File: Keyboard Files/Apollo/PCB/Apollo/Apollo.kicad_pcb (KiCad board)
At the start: 2 copper layers, 309.8 x 159.1 mm, 198 parts, among them J1 AVR-ISP-6, J10 Conn_01x01, J11 Conn_01x01, J12 Conn_01x01, J13 Conn_01x01, J14 Conn_01x01, J15 Conn_01x01, J16 Conn_01x01, J2 AVR-ISP-6, J3 Conn_01x01, J4 Conn_01x01, J5 Conn_01x01, J6 Conn_01x01, J7 Conn_01x01, J8 Conn_01x01, J9 Conn_01x01, SW1 SW_Push, SW2 SW_Push, U1 PRTR5V0U2X, U2 ATmega32U4-MU, U3 PRTR5V0U2X, U4 ATmega32U4-MU, Y1 Crystal_GND24_Small, Y2 Crystal_GND24_Small

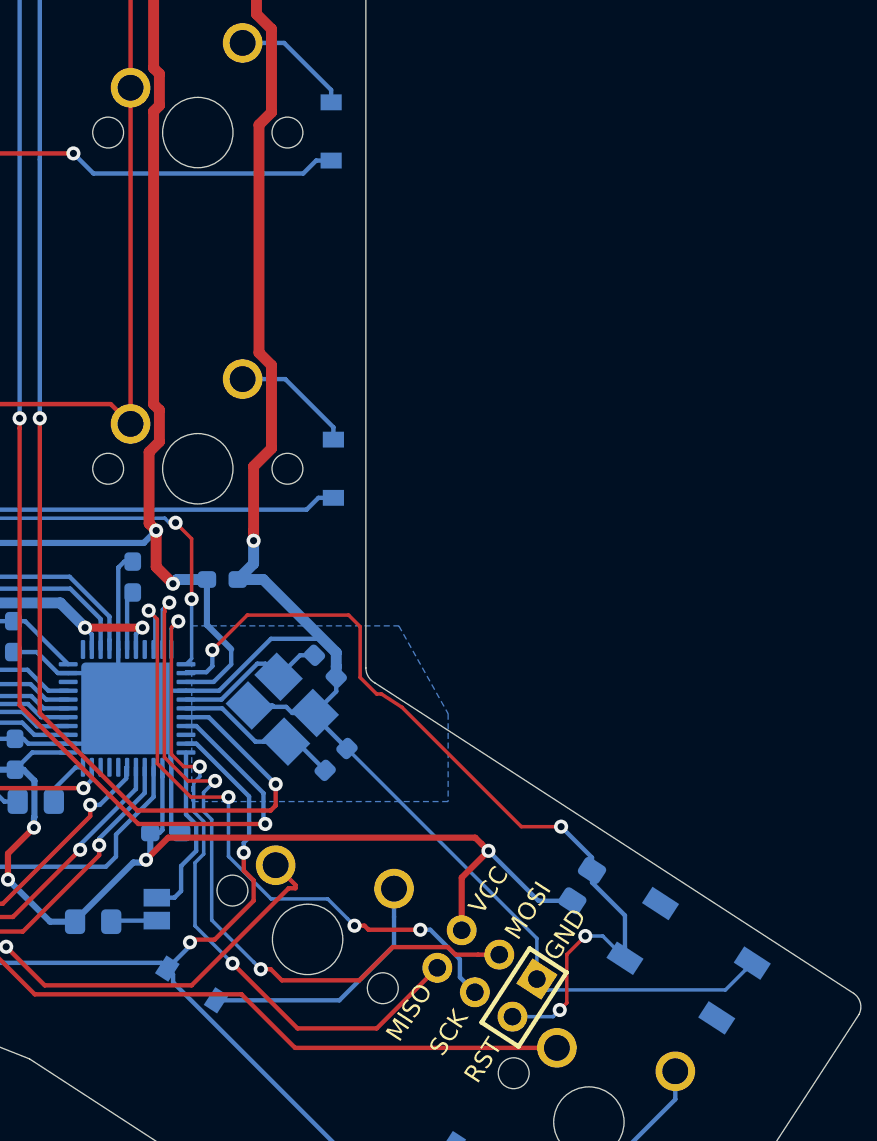
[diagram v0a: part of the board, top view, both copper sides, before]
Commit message: Increase Apollo plate bezel
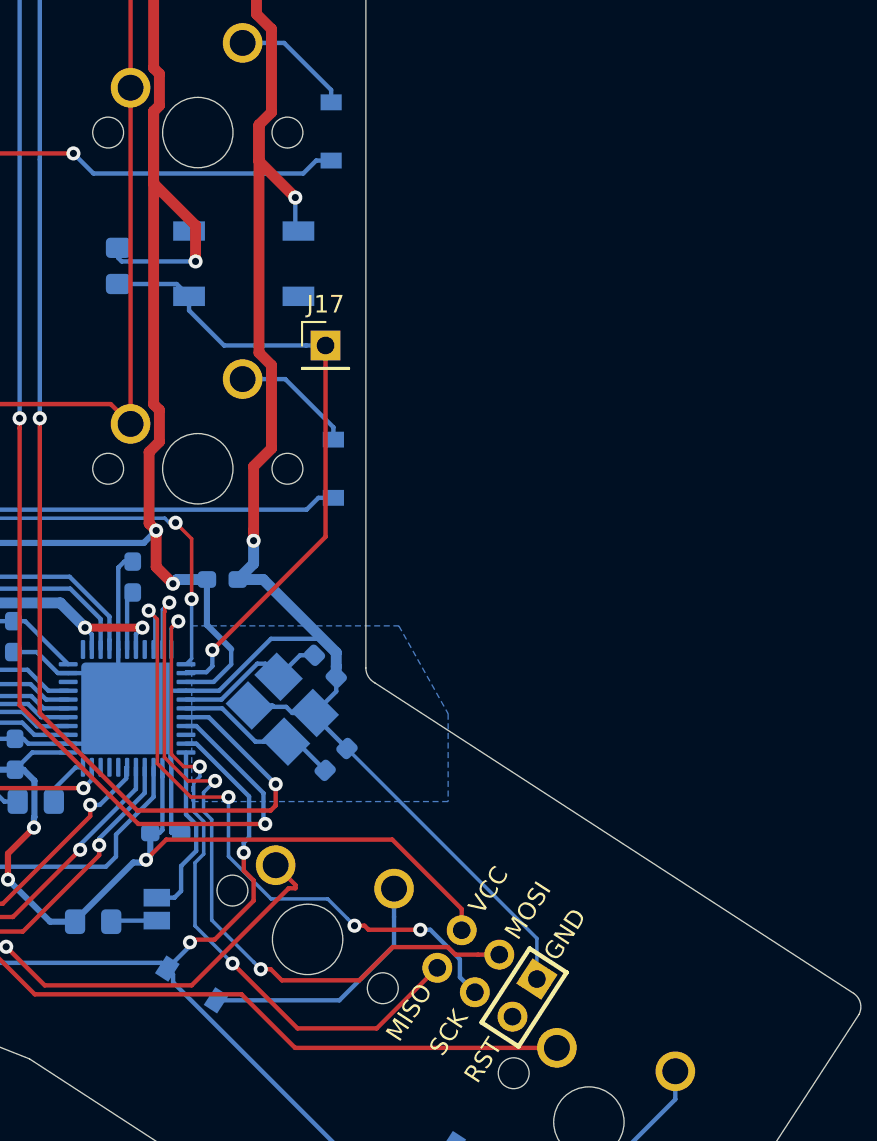
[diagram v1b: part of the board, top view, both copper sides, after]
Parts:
- added J17: Conn_01x01, Connector_PinHeader_2.54mm:PinHeader_1x01_P2.54mm_Vertical, F.Cu at (180.9, 123.5)
- moved SW1 46.9 mm to (176.3, 118.9), turned to 0 degrees
- moved R2 43.9 mm to (169.2, 119.0), turned to 90 degrees
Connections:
- J1 pad 5: RST -> Net-(J1-Pad5)
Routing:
- net RST: track 49.3 -> 36.2 mm, vias 4 -> 1
- net GND: track 370.3 -> 364.1 mm, vias 1 -> 2
- net +5V: track 279.2 -> 283.2 mm

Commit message: Update Apollo plate for 1.5u
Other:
- board size 309.8 x 159.1 mm -> 309.9 x 159.1 mm

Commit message: Add Aurora Keyboard
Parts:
- removed J1: AVR-ISP-6, Molex-0548190589:Reset_Pretty-Mask
- removed J10, J11, J12, J13, J14, J15, J16, J4, J5, J6, J7, J8, J9: Conn_01x01, locallib:breakaway-mousebites
- removed J17: Conn_01x01, Connector_PinHeader_2.54mm:PinHeader_1x01_P2.54mm_Vertical
- removed JP1, JP2: Jumper_NO, Jumper:SolderJumper-2_P1.3mm_Open_Pad1.0x1.5mm
- removed U3: PRTR5V0U2X, locallib:SOT143B
- removed U4: ATmega32U4-MU, Package_DFN_QFN:QFN-44-1EP_7x7mm_P0.5mm_EP5.2x5.2mm
- added TP1: TestPoint, Connector_PinHeader_2.00mm:PinHeader_1x01_P2.00mm_Vertical, F.Cu at (172.2, 67.1)
- added TP2: TestPoint, Connector_PinHeader_2.00mm:PinHeader_1x01_P2.00mm_Vertical, F.Cu at (154.0, 63.4)
- added TP3: TestPoint, Connector_PinHeader_2.00mm:PinHeader_1x01_P2.00mm_Vertical, F.Cu at (256.9, 65.6)
- added TP4: TestPoint, Connector_PinHeader_2.00mm:PinHeader_1x01_P2.00mm_Vertical, F.Cu at (273.3, 63.1)
- C1, C10, C11, C12, C13, C14, C2, C3, C4, C5, C6, C7, C8, C9: footprint Capacitor_SMD:C_0603_1608Metric_Pad1.05x0.95mm_HandSolder -> Capacitor_SMD:C_0805_2012Metric_Pad1.15x1.40mm_HandSolder
- D13, D45: value Schottky -> D_Small
- D39, D7: value D_Small -> Schottky
- F1, F2: value 500mA -> Polyfuse_Small; footprint Fuse:Fuse_0603_1608Metric_Pad1.05x0.95mm_HandSolder -> Fuse:Fuse_0805_2012Metric_Pad1.15x1.40mm_HandSolder
- J2: value AVR-ISP-6 -> Conn_01x04; footprint Molex-0548190589:Reset_Pretty-Mask -> Connector_PinHeader_2.00mm:PinHeader_1x04_P2.00mm_Vertical
- J3: value Conn_01x01 -> Conn_01x04; footprint locallib:breakaway-mousebites -> Connector_PinHeader_2.00mm:PinHeader_1x04_P2.00mm_Vertical
- R11, R2: value 10k -> 22
- R13, R4: value 22 -> 5.1k
- R15, R6: value 5.1k -> 10k
- U1: value PRTR5V0U2X -> ATmega32U4-MU; footprint locallib:SOT143B -> Package_QFP:TQFP-44_10x10mm_P0.8mm
- U2: footprint Package_DFN_QFN:QFN-44-1EP_7x7mm_P0.5mm_EP5.2x5.2mm -> Package_QFP:TQFP-44_10x10mm_P0.8mm
- Y1, Y2: footprint Crystal:Crystal_SMD_3225-4Pin_3.2x2.5mm_HandSoldering -> Crystal:Crystal_SMD_3225-4Pin_3.2x2.5mm
- moved J3 213.0 mm to (262.7, 155.0), turned to 270 degrees
- moved R11 134.7 mm to (341.7, 74.8), turned to 90 degrees
- moved R6 122.6 mm to (174.5, 147.3), turned to 90 degrees
- moved U1 103.9 mm to (166.1, 140.0)
- moved D13 97.5 mm to (181.3, 92.0)
- moved R15 95.4 mm to (258.5, 128.1)
- moved U2 93.7 mm to (263.3, 140.1), turned to 90 degrees
- moved R2 90.1 mm to (89.5, 76.9)
- moved D39 90.0 mm to (336.7, 86.1)
- moved J2 78.3 mm to (167.4, 123.8), turned to 90 degrees
- moved D44 39.7 mm to (323.1, 94.4)
- moved D8 39.0 mm to (66.1, 94.5)
- moved R1 37.2 mm to (169.7, 119.0), turned to 270 degrees
- moved D12 34.4 mm to (146.7, 89.8)
- moved D40 34.4 mm to (247.1, 91.8)
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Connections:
- net VDD renamed Net-(F2-Pad2)
- D13 pad 1: +5V -> Row1
- D13 pad 2: VBUS -> Net-(D13-Pad2)
- D39 pad 1: Row1_1 -> +5VA
- D45 pad 1: +5VA -> Row1_1
- D45 pad 2: VPP -> Net-(D45-Pad2)
- D7 pad 1: Row1 -> +5V
- F1 pad 1: VBUS -> Net-(D7-Pad2)
- F1 pad 2: VCC -> Net-(F1-Pad2)
- F2 pad 1: VPP -> Net-(D39-Pad2)
- J2 pad 1: MISO_1 -> RST
- J2 pad 2: +5VA -> SCK
- J2 pad 3: SCK_1 -> MOSI
- J2 pad 4: MOSI_1 -> MISO
- MX10 pad 2: Net-(D10-Pad2) -> Net-(D11-Pad2)
- MX11 pad 2: Net-(D11-Pad2) -> Net-(D12-Pad2)
- MX12 pad 2: Net-(D12-Pad2) -> Net-(D13-Pad2)
- MX38 pad 2: Net-(D39-Pad2) -> Net-(D40-Pad2)
- MX39 pad 2: Net-(D40-Pad2) -> Net-(D41-Pad2)
- MX40 pad 2: Net-(D41-Pad2) -> Net-(D42-Pad2)
- MX41 pad 2: Net-(D42-Pad2) -> Net-(D43-Pad2)
- MX42 pad 2: Net-(D43-Pad2) -> Net-(D44-Pad2)
- MX43 pad 2: Net-(D44-Pad2) -> Net-(D45-Pad2)
- MX64 pad 2: Net-(D7-Pad2) -> Net-(D8-Pad2)
- MX69 pad 2: Net-(D44-Pad2) -> Net-(D45-Pad2)
- MX7 pad 2: Net-(D7-Pad2) -> Net-(D8-Pad2)
- MX8 pad 2: Net-(D8-Pad2) -> Net-(D9-Pad2)
- MX9 pad 2: Net-(D9-Pad2) -> Net-(D10-Pad2)
- R1 pad 1: +5V -> RST
- R1 pad 2: Net-(JP1-Pad2) -> +5V
- R10 pad 1: GNDA -> RST_1
- R10 pad 2: Net-(JP2-Pad2) -> +5VA
- R11 pad 1: RST_1 -> D1_+
- R11 pad 2: +5VA -> Net-(R11-Pad2)
- R12 pad 1: D1_+ -> D1_-
- R13 pad 1: D1_- -> Net-(R13-Pad1)
- R13 pad 2: Net-(R13-Pad2) -> GNDA
- R15 pad 1: Net-(R15-Pad1) -> GNDA
- R15 pad 2: GNDA -> Net-(R15-Pad2)
- R2 pad 1: RST -> D+
- R2 pad 2: +5V -> Net-(R2-Pad2)
- R3 pad 1: D+ -> D-
- R4 pad 1: D- -> Net-(R4-Pad1)
- R4 pad 2: Net-(R4-Pad2) -> GND
- R6 pad 1: Net-(R6-Pad1) -> +5V
- R6 pad 2: GND -> Net-(R6-Pad2)
- U1 pad 1: GND -> CapsLED
- U1 pad 2: Net-(R3-Pad2) -> +5V
- U1 pad 3: Net-(R4-Pad2) -> D-
- U1 pad 4: VCC -> D+
- U2 pad 1: Net-(U2-Pad1) -> Row4_1
- U2 pad 10: MOSI -> MOSI_1
- U2 pad 11: MISO -> MISO_1
- U2 pad 12: CapsLED -> Net-(U2-Pad12)
- U2 pad 13: RST -> RST_1
- U2 pad 14: +5V -> +5VA
- U2 pad 15: GND -> GNDA
- U2 pad 16: Net-(C6-Pad1) -> Net-(C13-Pad1)
- U2 pad 17: Net-(C5-Pad1) -> Net-(C12-Pad1)
- U2 pad 18: SCL -> SCL_1
- U2 pad 19: SDA -> SDA_1
- U2 pad 2: VBUS -> +5VA
- U2 pad 21: Row4 -> Net-(U2-Pad21)
- U2 pad 22: HDETECT -> Net-(R15-Pad2)
- U2 pad 23: GND -> GNDA
- U2 pad 24: +5V -> +5VA
- U2 pad 25: Col4 -> Net-(U2-Pad25)
- U2 pad 26: Col3 -> Col1_1
- U2 pad 27: Col2 -> Row3_1
- U2 pad 28: Col1 -> Row2_1
- U2 pad 29: Net-(U2-Pad29) -> Row1_1
- U2 pad 3: D- -> D1_-
- U2 pad 30: Net-(U2-Pad30) -> Row0_1
- U2 pad 31: Net-(U2-Pad31) -> Col6_1
- U2 pad 32: Col0 -> Net-(U2-Pad32)
- U2 pad 33: Net-(R7-Pad2) -> Net-(R16-Pad2)
- U2 pad 34: +5V -> +5VA
- U2 pad 35: GND -> GNDA
- U2 pad 36: Row0 -> Net-(U2-Pad36)
- U2 pad 37: Row1 -> Net-(U2-Pad37)
- U2 pad 38: Row2 -> Col5_1
- U2 pad 39: Row3 -> Col4_1
- U2 pad 4: D+ -> D1_+
- U2 pad 40: Col5 -> Col2_1
- U2 pad 41: Col6 -> Col3_1
- U2 pad 43: GND -> GNDA
- U2 pad 44: +5V -> +5VA
- U2 pad 5: GND -> GNDA
- U2 pad 6: Net-(C7-Pad1) -> Net-(C14-Pad1)
- U2 pad 7: VBUS -> +5VA
- U2 pad 8: Net-(U2-Pad8) -> Col0_1
- U2 pad 9: SCK -> SCK_1
- USB1 pad 10: Net-(R5-Pad1) -> Net-(R4-Pad1)
- USB1 pad 11: VCC -> Net-(F1-Pad2)
- USB1 pad 2: VCC -> Net-(F1-Pad2)
- USB1 pad 4: Net-(R6-Pad1) -> Net-(R5-Pad1)
- USB1 pad 5: Net-(R4-Pad2) -> Net-(R3-Pad2)
- USB1 pad 6: Net-(R3-Pad2) -> Net-(R2-Pad2)
- USB1 pad 7: Net-(R4-Pad2) -> Net-(R3-Pad2)
- USB1 pad 8: Net-(R3-Pad2) -> Net-(R2-Pad2)
- USB3 pad 10: Net-(R14-Pad1) -> Net-(R13-Pad1)
- USB3 pad 4: Net-(R15-Pad1) -> Net-(R14-Pad1)
- USB3 pad 5: Net-(R13-Pad2) -> Net-(R12-Pad2)
- USB3 pad 6: Net-(R12-Pad2) -> Net-(R11-Pad2)
- USB3 pad 7: Net-(R13-Pad2) -> Net-(R12-Pad2)
- USB3 pad 8: Net-(R12-Pad2) -> Net-(R11-Pad2)
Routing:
- net VBUS: track 150.9 -> 0.00 mm, vias 6 -> 0
- net VPP: track 146.7 -> 0.00 mm, vias 5 -> 0
- net +5V: track 283.2 -> 327.6 mm, vias 16 -> 9
- net GNDA: track 308.1 -> 267.9 mm
- net +5VA: track 264.5 -> 301.0 mm, vias 9 -> 7
- net Col6: track 79.5 -> 44.2 mm, vias 3 -> 1
- net GND: track 364.1 -> 397.1 mm
- net MOSI: track 42.2 -> 11.3 mm, vias 3 -> 0
- net MISO: track 38.8 -> 12.1 mm, vias 3 -> 0
- net VCC: track 26.3 -> 0.00 mm, vias 2 -> 0
- net Net-(F1-Pad2): track 0.00 -> 26.2 mm, vias 0 -> 2
- net SCK: track 37.4 -> 11.7 mm, vias 4 -> 0
- net SCL: track 106.1 -> 83.0 mm
- net SDA: track 108.9 -> 86.7 mm
- net SCK_1: track 32.0 -> 10.0 mm, vias 1 -> 0
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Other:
- board size 309.9 x 159.1 mm -> 309.4 x 125.5 mm
- board text added: "LEFT"
- board text added: "RIGHT"
